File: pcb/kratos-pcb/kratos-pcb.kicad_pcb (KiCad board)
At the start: 2 copper layers, 100 x 100 mm, 28 parts, among them IC2 SN74HC595N, J1 Barrel_Jack_Switch_Pin3Ring, J2 Screw_Terminal_01x04, J3 Screw_Terminal_01x04, Q2 2N2222A, Q3 2N2222A, SW1 SW_Push, U1 ESP32-DEVKIT-V1, U2 ULN2803A, U3 ULN2803A

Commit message: kicad
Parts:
- C1: footprint Capacitor_THT:C_Disc_D3.0mm_W1.6mm_P2.50mm -> Capacitor_THT:CP_Radial_D4.0mm_P1.50mm
- moved Q3 52.7 mm to (164.3, 58.6), turned to 0 degrees
- moved Q2 50.8 mm to (153.0, 58.4), turned to 0 degrees
- moved R5 43.8 mm to (161.3, 64.8), turned to -90 degrees
- moved R4 43.1 mm to (149.9, 64.8), turned to -90 degrees
- moved R7 40.7 mm to (167.0, 69.8), turned to 90 degrees
- moved R6 35.0 mm to (155.6, 69.8), turned to 90 degrees
- moved IC2 24.2 mm to (142.9, 104.3), turned to -90 degrees
- moved U3 16.7 mm to (145.4, 88.3), turned to 90 degrees
- moved U2 13.4 mm to (168.3, 116.2), turned to 90 degrees
- moved C1 10.9 mm to (123.4, 68.6)
- moved C2 9.71 mm to (116.8, 62.9)
- moved R1 9.71 mm to (119.4, 59.1)
- moved VR1 9.71 mm to (123.8, 62.9)
- moved R2 9.55 mm to (132.1, 59.1)
- moved SW1 6.48 mm to (134.6, 139.7)

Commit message: ki
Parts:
- R7: value R -> 1k
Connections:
- C2 pad 1: Net-(VR1-VIN) -> +12V
- J1 pad 1: Net-(VR1-VIN) -> +12V
- LOCK_1 pad 1: unconnected-(LOCK_1-Pin_1-Pad1) -> +12V
- LOCK_1 pad 2: unconnected-(LOCK_1-Pin_2-Pad2) -> Net-(LOCK_1-Pin_2)
- LOCK_2 pad 1: unconnected-(LOCK_2-Pin_1-Pad1) -> +12V
- LOCK_2 pad 2: unconnected-(LOCK_2-Pin_2-Pad2) -> Net-(LOCK_2-Pin_2)
- Q2 pad 1: Net-(Q2-Pad1) -> GND
- Q2 pad 3: unconnected-(Q2-Pad3) -> Net-(LOCK_2-Pin_2)
- Q3 pad 1: Net-(Q3-Pad1) -> GND
- Q3 pad 3: unconnected-(Q3-Pad3) -> Net-(LOCK_1-Pin_2)
- VR1 pad 3: Net-(VR1-VIN) -> +12V
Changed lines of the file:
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@@
   (net 1 "+5V")
   (net 2 "GND")
-  (net 3 "Net-(VR1-VIN)")
+  (net 3 "+12V")
   (net 4 "DHT_DATA")
   (net 5 "Net-(FREE_OUTPUT1-Pin_1)")
@@
   (net 16 "Net-(Q2-Pad1)")
   (net 17 "Net-(Q2-Pad2)")
-  (net 18 "unconnected-(Q2-Pad3)")
+  (net 18 "Net-(LOCK_1-Pin_2)")
   (net 19 "Net-(Q3-Pad1)")
   (net 20 "Net-(Q3-Pad2)")
-  (net 21 "unconnected-(Q3-Pad3)")
+  (net 21 "Net-(LOCK_2-Pin_2)")
   (net 22 "Net-(VR1-ADJ)")
   (net 23 "unconnected-(R4-Pad2)")
@@
   (net 66 "Net-(J2-Pin_1)")
   (net 67 "Net-(J2-Pin_2)")
-  (net 68 "unconnected-(LOCK_1-Pin_1-Pad1)")
-  (net 69 "unconnected-(LOCK_1-Pin_2-Pad2)")
-  (net 70 "unconnected-(LOCK_2-Pin_1-Pad1)")
-  (net 71 "unconnected-(LOCK_2-Pin_2-Pad2)")
-  (net 72 "unconnected-(J1-Pad2)")
+  (net 68 "unconnected-(J1-Pad2)")
   (footprint "ULN2803A:ULN2803A" (layer "F.Cu")
     (at 168.275 116.205 90)
@@
       (stroke (width 0.1) (type solid)) (layer "F.Fab"))
     (pad "1" thru_hole rect (at 0 0 180) (size 3 3) (drill 1.52) (layers "*.Cu" "*.Mask")
-      (net 68 "unconnected-(LOCK_1-Pin_1-Pad1)") (pinfunction "Pin_1") (pintype "passive"))
+      (net 3 "+12V") (pinfunction "Pin_1") (pintype "passive"))
     (pad "2" thru_hole circle (at 5.08 0 180) (size 3 3) (drill 1.52) (layers "*.Cu" "*.Mask")
-      (net 69 "unconnected-(LOCK_1-Pin_2-Pad2)") (pinfunction "Pin_2") (pintype "passive"))
+      (net 18 "Net-(LOCK_1-Pin_2)") (pinfunction "Pin_2") (pintype "passive"))
     (model "${KICAD6_3DMODEL_DIR}/TerminalBlock.3dshapes/TerminalBlock_bornier-2_P5.08mm.wrl"
       (offset (xyz 2.539999962 0 0))
@@
       (stroke (width 0.2) (type solid)) (fill none) (layer "F.Fab"))
     (pad "1" thru_hole rect (at -2.54 2.33) (size 1.298 1.298) (drill 0.79) (layers "*.Cu" "*.Mask")
-      (net 19 "Net-(Q3-Pad1)") (pintype "passive") (solder_mask_margin 0.102))
+      (net 2 "GND") (pintype "passive") (solder_mask_margin 0.102))
     (pad "2" thru_hole circle (at 0 2.33) (size 1.298 1.298) (drill 0.79) (layers "*.Cu" "*.Mask")
       (net 20 "Net-(Q3-Pad2)") (pintype "passive") (solder_mask_margin 0.102))
     (pad "3" thru_hole circle (at 2.54 2.33) (size 1.298 1.298) (drill 0.79) (layers "*.Cu" "*.Mask")
-      (net 21 "unconnected-(Q3-Pad3)") (pintype "passive") (solder_mask_margin 0.102))
+      (net 18 "Net-(LOCK_1-Pin_2)") (pintype "passive") (solder_mask_margin 0.102))
     (model "${KIPRJMOD}/components/2N2222A/2N2222A.step"
       (offset (xyz 0 -2 6))
@@
       (net 1 "+5V") (pinfunction "VOUT") (pintype "output") (solder_mask_margin 0.102))
     (pad "3" thru_hole circle (at 2.54 0 180) (size 1.86 1.86) (drill 1.24) (layers "*.Cu" "*.Mask")
-      (net 3 "Net-(VR1-VIN)") (pinfunction "VIN") (pintype "input") (solder_mask_margin 0.102))
+      (net 3 "+12V") (pinfunction "VIN") (pintype "input") (solder_mask_margin 0.102))
     (model "${KIPRJMOD}/components/LM317T/LM317T.step"
       (offset (xyz 0 0 0))
@@
       (stroke (width 0.2) (type solid)) (fill none) (layer "F.Fab"))
     (pad "1" thru_hole rect (at -2.54 2.33) (size 1.298 1.298) (drill 0.79) (layers "*.Cu" "*.Mask")
-      (net 16 "Net-(Q2-Pad1)") (pintype "passive") (solder_mask_margin 0.102))
+      (net 2 "GND") (pintype "passive") (solder_mask_margin 0.102))
     (pad "2" thru_hole circle (at 0 2.33) (size 1.298 1.298) (drill 0.79) (layers "*.Cu" "*.Mask")
       (net 17 "Net-(Q2-Pad2)") (pintype "passive") (solder_mask_margin 0.102))
     (pad "3" thru_hole circle (at 2.54 2.33) (size 1.298 1.298) (drill 0.79) (layers "*.Cu" "*.Mask")
-      (net 18 "unconnected-(Q2-Pad3)") (pintype "passive") (solder_mask_margin 0.102))
+      (net 21 "Net-(LOCK_2-Pin_2)") (pintype "passive") (solder_mask_margin 0.102))
     (model "${KIPRJMOD}/components/2N2222A/2N2222A.step"
       (offset (xyz 0 -2 6.5))
@@
       (stroke (width 0.1) (type solid)) (layer "F.Fab"))
     (pad "1" thru_hole rect (at 0 0 180) (size 3 3) (drill 1.52) (layers "*.Cu" "*.Mask")
-      (net 70 "unconnected-(LOCK_2-Pin_1-Pad1)") (pinfunction "Pin_1") (pintype "passive"))
+      (net 3 "+12V") (pinfunction "Pin_1") (pintype "passive"))
     (pad "2" thru_hole circle (at 5.08 0 180) (size 3 3) (drill 1.52) (layers "*.Cu" "*.Mask")
-      (net 71 "unconnected-(LOCK_2-Pin_2-Pad2)") (pinfunction "Pin_2") (pintype "passive"))
+      (net 21 "Net-(LOCK_2-Pin_2)") (pinfunction "Pin_2") (pintype "passive"))
     (model "${KICAD6_3DMODEL_DIR}/TerminalBlock.3dshapes/TerminalBlock_bornier-2_P5.08mm.wrl"
       (offset (xyz 2.539999962 0 0))
@@
       (stroke (width 0.1) (type solid)) (layer "F.Fab"))
     (pad "1" thru_hole rect (at 0 0) (size 3.5 3.5) (drill oval 1 3) (layers "*.Cu" "*.Mask")
-      (net 3 "Net-(VR1-VIN)") (pintype "passive"))
+      (net 3 "+12V") (pintype "passive"))
     (pad "2" thru_hole roundrect (at -6 0) (size 3 3.5) (drill oval 1 3) (layers "*.Cu" "*.Mask") (roundrect_rratio 0.25)
-      (net 72 "unconnected-(J1-Pad2)") (pintype "passive+no_connect"))
+      (net 68 "unconnected-(J1-Pad2)") (pintype "passive+no_connect"))
     (pad "3" thru_hole roundrect (at -3 4.7) (size 3.5 3.5) (drill oval 3 1) (layers "*.Cu" "*.Mask") (roundrect_rratio 0.25)
       (net 2 "GND") (pintype "passive"))
@@
         (effects (font (size 1 1) (thickness 0.15)))
     )
-    (fp_text value "R" (at 2.54 1.92 90) (layer "F.Fab")
+    (fp_text value "1k" (at 2.54 1.92 90) (layer "F.Fab")
         (effects (font (size 1 1) (thickness 0.15)))
     )
@@
       (stroke (width 0.1) (type solid)) (layer "F.Fab"))
     (pad "1" thru_hole circle (at 0 0 270) (size 1.6 1.6) (drill 0.8) (layers "*.Cu" "*.Mask")
-      (net 3 "Net-(VR1-VIN)") (pintype "passive"))
+      (net 3 "+12V") (pintype "passive"))
     (pad "2" thru_hole circle (at 2.5 0 270) (size 1.6 1.6) (drill 0.8) (layers "*.Cu" "*.Mask")
       (net 2 "GND") (pintype "passive"))

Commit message: ## updatee
- gitignor
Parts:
- removed R4, R5: R, Resistor_THT:R_Axial_DIN0204_L3.6mm_D1.6mm_P5.08mm_Horizontal
- added LEDS1: Screw_Terminal_01x03, TerminalBlock_4Ucon:TerminalBlock_4Ucon_1x03_P3.50mm_Horizontal, F.Cu at (190.5, 80.3)
- R6: value R -> 1K
- moved LOCK_2 91.2 mm to (157.5, 48.3)
- moved LOCK_1 91.2 mm to (170.2, 48.3)
- moved SDOOR_1 42.0 mm to (147.3, 139.7), turned to 180 degrees
- moved SDOOR_2 32.2 mm to (160.0, 139.7), turned to 180 degrees
- moved U3 23.6 mm to (166.4, 77.5), turned to 0 degrees
- moved U2 22.5 mm to (146.1, 113.0), turned to 0 degrees
- moved J3 17.2 mm to (190.5, 132.1)
- moved IC2 12.9 mm to (142.2, 91.4)
- moved R6 12.8 mm to (149.9, 58.4), turned to 0 degrees
- moved R7 12.3 mm to (162.6, 58.4), turned to 0 degrees
- moved C1 10.5 mm to (113.3, 66.0)
- moved R8 9.09 mm to (104.1, 83.8)
- moved FAN1 8.26 mm to (167.6, 139.4)
- moved C2 6.29 mm to (112.4, 58.4)
- moved R2 6.29 mm to (127.6, 54.6)
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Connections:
- FAN1 pad 1: FAN_PWM -> VCC
- FAN1 pad 2: GND -> FAN_PWM
- IC2 pad 6: /EXPANSION DRIVERS/G -> LOCKER_1
- IC2 pad 7: /EXPANSION DRIVERS/H -> LOCKER_2
- LOCK_1 pad 1: +12V -> Net-(LOCK_1-Pin_1)
- LOCK_1 pad 2: Net-(LOCK_1-Pin_2) -> +12V
- LOCK_2 pad 1: +12V -> Net-(LOCK_2-Pin_1)
- LOCK_2 pad 2: Net-(LOCK_2-Pin_2) -> +12V
- Q2 pad 3: Net-(LOCK_2-Pin_2) -> Net-(LOCK_2-Pin_1)
- Q3 pad 3: Net-(LOCK_1-Pin_2) -> Net-(LOCK_1-Pin_1)
- U1 pad 10: GREEN-LED-2 -> unconnected-(U1-D19-Pad10)
- U1 pad 11: BLUE-LED-2 -> unconnected-(U1-D21-Pad11)
- U1 pad 15: SHIFT_SER -> DS
- U1 pad 26: SH_CP -> BLUE-LED-2
- U1 pad 28: DS -> GREEN-LED-2
- U1 pad 3: ST_CP -> unconnected-(U1-D15-Pad3)
- U1 pad 8: SHIFT_RCKL -> ST_CP
- U1 pad 9: SHIFT_SRCLOCK -> SH_CP
- U3 pad 1: /EXPANSION DRIVERS/H -> unconnected-(U3-I1-Pad1)
- U3 pad 14: LOCKER_1 -> Net-(LEDS1-Pin_3)
- U3 pad 15: LOCKER_2 -> Net-(LEDS1-Pin_2)
- U3 pad 16: Net-(FREE_OUTPUT1-Pin_3) -> Net-(LEDS1-Pin_1)
- U3 pad 17: Net-(FREE_OUTPUT1-Pin_2) -> unconnected-(U3-O2-Pad17)
- U3 pad 18: Net-(FREE_OUTPUT1-Pin_1) -> unconnected-(U3-O1-Pad18)
- U3 pad 2: /EXPANSION DRIVERS/G -> unconnected-(U3-I2-Pad2)

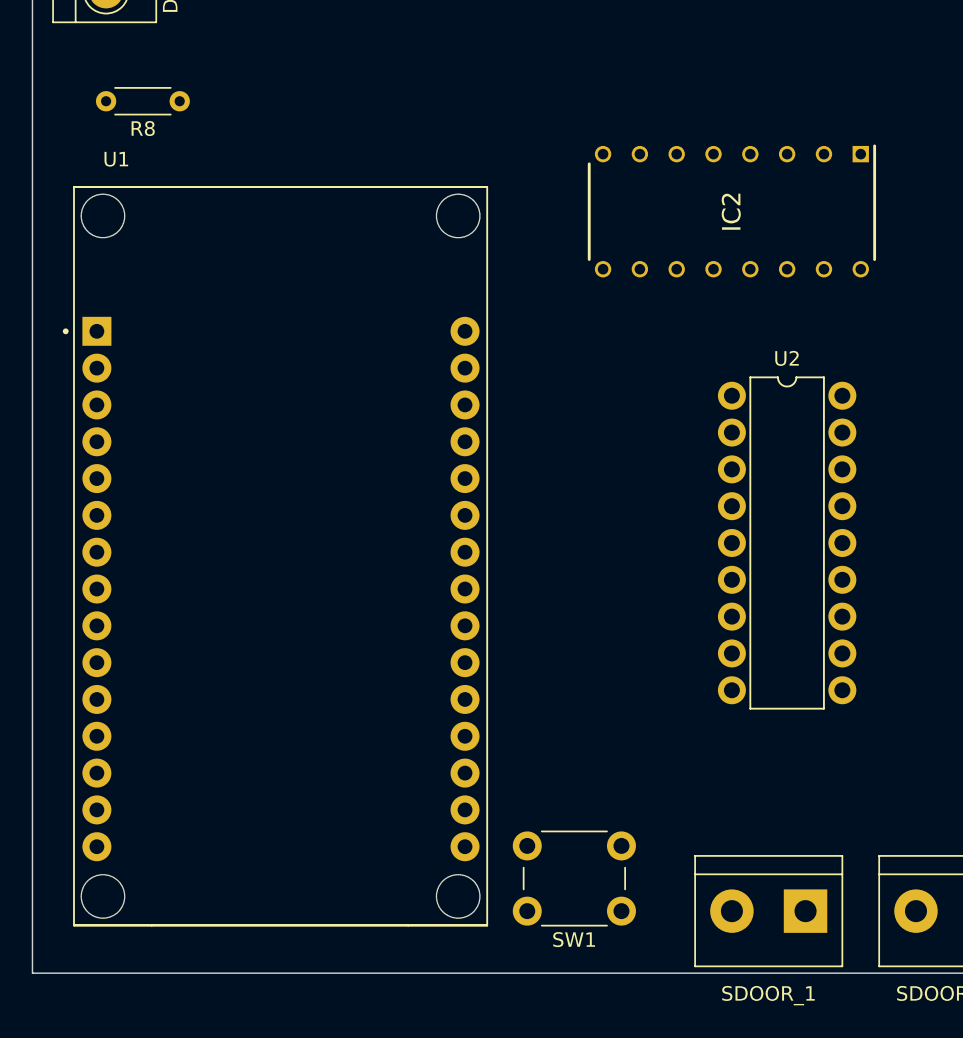
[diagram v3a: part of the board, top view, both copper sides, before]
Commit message: ### added - bitshift logic
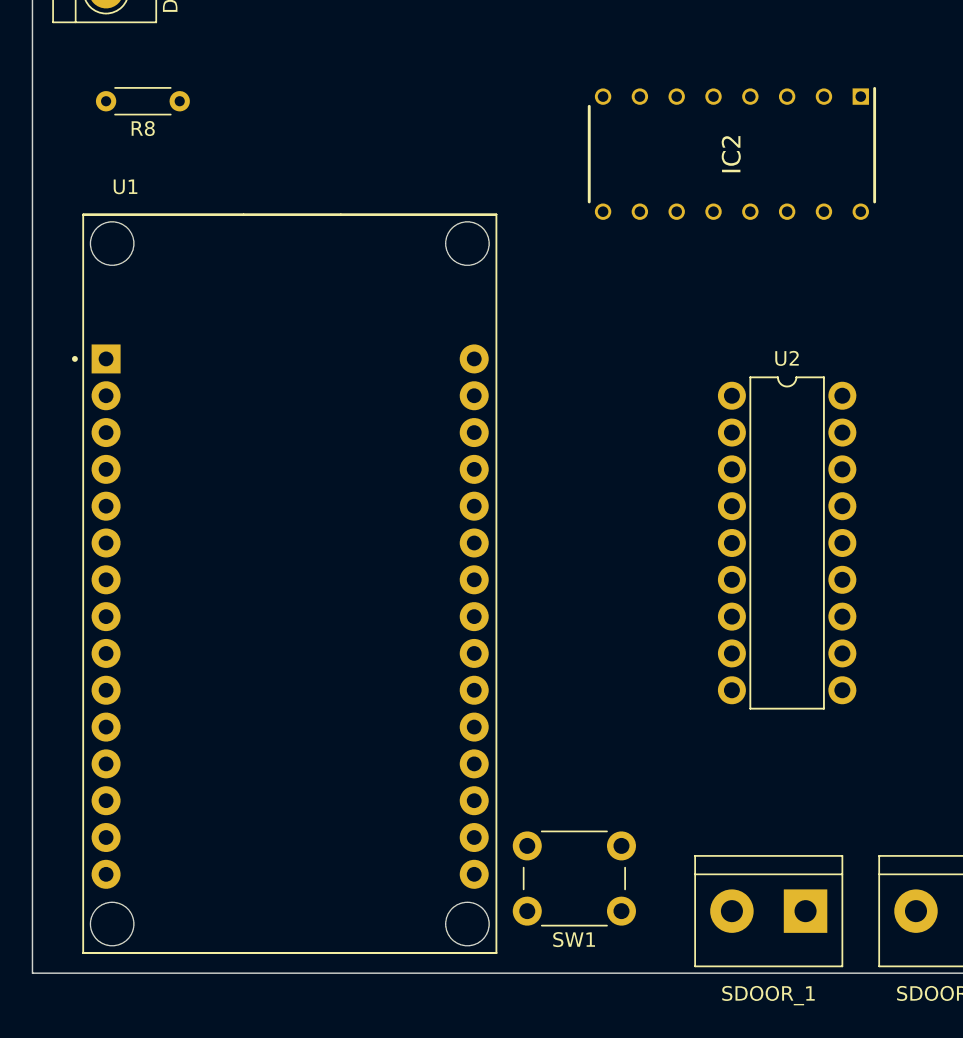
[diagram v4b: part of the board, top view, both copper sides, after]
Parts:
- moved IC2 3.97 mm to (142.2, 87.5)
- moved U1 2.01 mm to (111.8, 117.1)
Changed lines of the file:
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@@
   )
   (footprint "ESP32-DEVKIT-V1:MODULE_ESP32_DEVKIT_V1" (layer "F.Cu")
-    (at 111.125 115.21)
+    (at 111.76 117.115)
     (property "Availability" "Not in stock")
     (property "Check_prices" "https://www.snapeda.com/parts/ESP32-DEVKIT-V1/Do+it/view-part/?ref=eda")
@@
       (polygon
         (pts
-          (xy 102.215 134.195)
-          (xy 119.905 134.195)
-          (xy 119.905 140.685)
-          (xy 102.215 140.685)
+          (xy 102.85 136.1)
+          (xy 120.54 136.1)
+          (xy 120.54 142.59)
+          (xy 102.85 142.59)
         )
       )
@@
       (polygon
         (pts
-          (xy 102.215 134.195)
-          (xy 119.905 134.195)
-          (xy 119.905 140.685)
-          (xy 102.215 140.685)
+          (xy 102.85 136.1)
+          (xy 120.54 136.1)
+          (xy 120.54 142.59)
+          (xy 102.85 142.59)
         )
       )
@@
       (polygon
         (pts
-          (xy 102.215 134.195)
-          (xy 119.905 134.195)
-          (xy 119.905 140.685)
-          (xy 102.215 140.685)
+          (xy 102.85 136.1)
+          (xy 120.54 136.1)
+          (xy 120.54 142.59)
+          (xy 102.85 142.59)
         )
       )
@@
   )
   (footprint "SN74HC595N:DIP794W53P254L1930H508Q16N" (layer "F.Cu")
-    (at 142.24 91.44 -90)
+    (at 142.24 87.47 -90)
     (descr "N (R-PDIP-T16)")
     (tags "Integrated Circuit")

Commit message: ### added
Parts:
- removed FREE_OUTPUT1: Screw_Terminal_01x03, TerminalBlock_4Ucon:TerminalBlock_4Ucon_1x03_P3.50mm_Horizontal
- removed J2, J3: Screw_Terminal_01x04, TerminalBlock:TerminalBlock_bornier-4_P5.08mm
- added LED-RGB-1.1: Screw_Terminal_01x02, TerminalBlock:TerminalBlock_bornier-2_P5.08mm, F.Cu at (189.6, 93.0)
- added LED-RGB-1.2: Screw_Terminal_01x02, TerminalBlock:TerminalBlock_bornier-2_P5.08mm, F.Cu at (189.7, 79.0)
- added LED-RGB-2.1: Screw_Terminal_01x02, TerminalBlock:TerminalBlock_bornier-2_P5.08mm, F.Cu at (189.7, 68.3)
- added LED-RGB-2.2: Screw_Terminal_01x02, TerminalBlock:TerminalBlock_bornier-2_P5.08mm, F.Cu at (189.9, 57.0)
- added REF**: PinHeader_1x01_P1.00mm_Vertical, Connector_PinHeader_1.00mm:PinHeader_1x01_P1.00mm_Vertical, F.Cu at (128.0, 92.2)
- added REF**: PinHeader_1x01_P1.00mm_Vertical, Connector_PinHeader_1.00mm:PinHeader_1x01_P1.00mm_Vertical, F.Cu at (162.3, 56.9)
- added REF**: PinHeader_1x01_P1.00mm_Vertical, Connector_PinHeader_1.00mm:PinHeader_1x01_P1.00mm_Vertical, F.Cu at (165.1, 45.7)
- added REF**: PinHeader_1x01_P1.00mm_Vertical, Connector_PinHeader_1.00mm:PinHeader_1x01_P1.00mm_Vertical, F.Cu at (119.1, 66.0)
- added REF**: PinHeader_1x01_P1.00mm_Vertical, Connector_PinHeader_1.00mm:PinHeader_1x01_P1.00mm_Vertical, F.Cu at (170.7, 84.8)
- added REF**: PinHeader_1x01_P1.00mm_Vertical, Connector_PinHeader_1.00mm:PinHeader_1x01_P1.00mm_Vertical, F.Cu at (162.1, 52.3)
- added REF**: PinHeader_1x01_P1.00mm_Vertical, Connector_PinHeader_1.00mm:PinHeader_1x01_P1.00mm_Vertical, F.Cu at (113.3, 99.6)
- added RFID1: Conn_01x04_Pin, Connector_PinHeader_2.00mm:PinHeader_1x04_P2.00mm_Vertical, F.Cu at (119.1, 45.6)
- moved SW1 100.5 mm to (170.3, 45.8), turned to 0 degrees
- moved LEDS1 92.6 mm to (98.0, 75.8)
- moved RELAYS1 91.7 mm to (98.0, 63.6), turned to -90 degrees
- moved LOCK_1 90.9 mm to (151.4, 137.2), turned to 0 degrees
- moved LOCK_2 90.8 mm to (140.0, 137.4), turned to 0 degrees
- moved J1 79.2 mm to (102.7, 129.9), turned to 90 degrees
- moved Q2 74.0 mm to (139.9, 125.7)
- moved Q3 73.9 mm to (154.3, 126.0)
- moved C2 65.7 mm to (103.8, 123.6), turned to 0 degrees
- moved R1 64.1 mm to (98.9, 116.6), turned to 90 degrees
- moved VR1 60.2 mm to (103.8, 116.6), turned to -90 degrees
- moved R6 59.5 mm to (139.7, 117.1), turned to -90 degrees
- moved R7 58.0 mm to (154.1, 115.8), turned to -90 degrees
- moved U1 58.0 mm to (145.4, 69.9)
- moved R2 56.7 mm to (103.9, 106.1)
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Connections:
- FAN1 pad 1: VCC -> +5V
- LOCK_1 pad 1: Net-(LOCK_1-Pin_1) -> +12V
- LOCK_1 pad 2: +12V -> Net-(LOCK_1-Pin_2)
- LOCK_2 pad 1: Net-(LOCK_2-Pin_1) -> +12V
- LOCK_2 pad 2: +12V -> Net-(LOCK_2-Pin_2)
- Q2 pad 3: Net-(LOCK_2-Pin_1) -> Net-(LOCK_2-Pin_2)
- Q3 pad 3: Net-(LOCK_1-Pin_1) -> Net-(LOCK_1-Pin_2)
- R8 pad 1: +3V3 -> +3.3V
- U1 pad 21: BLUE-LED -> FAN_PWM_DRIVER
- U1 pad 22: GREEN-LED -> BLUE-LED
- U1 pad 23: RED-LED -> GREEN-LED
- U1 pad 25: FAN_PWM_DRIVER -> RED-LED
- U2 pad 1: RED-LED -> GREEN-LED-2
- U2 pad 2: GREEN-LED -> RED-LED-2
- U2 pad 3: BLUE-LED -> BLUE-LED-2
- U2 pad 4: RED-LED-2 -> RED-LED
- U2 pad 5: GREEN-LED-2 -> GREEN-LED
- U2 pad 6: BLUE-LED-2 -> BLUE-LED
- U3 pad 11: Net-(RELAYS1-Pin_3) -> Net-(RELAYS1-Pin_1)
- U3 pad 13: Net-(RELAYS1-Pin_1) -> Net-(RELAYS1-Pin_3)
- U3 pad 14: Net-(LEDS1-Pin_3) -> Net-(LEDS1-Pin_1)
- U3 pad 16: Net-(LEDS1-Pin_1) -> Net-(LEDS1-Pin_3)
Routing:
- net +5V: track 0.00 -> 213.6 mm
- net GND: track 0.00 -> 196.2 mm
- net +3.3V: track 0.00 -> 133.0 mm
- net +12V: track 0.00 -> 66.8 mm
- net Net-(U1-EN): track 0.00 -> 61.1 mm
- net SDOOR1: track 0.00 -> 59.5 mm
- net LOCKER_1: track 0.00 -> 53.8 mm
- net SDOOR2: track 0.00 -> 48.5 mm
- net LOCKER_2: track 0.00 -> 41.1 mm
- net DHT_DATA: track 0.00 -> 38.7 mm
- net FAN_PWM: track 0.00 -> 32.0 mm
- net Net-(LED-RGB-1.1-Pin_2): track 0.00 -> 25.5 mm
- net DS: track 0.00 -> 21.0 mm
- net Net-(LED-RGB-1.2-Pin_1): track 0.00 -> 19.7 mm
- net Net-(LED-RGB-2.2-Pin_2): track 0.00 -> 19.1 mm
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
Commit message: removed
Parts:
- removed REF** (x7): PinHeader_1x01_P1.00mm_Vertical, Connector_PinHeader_1.00mm:PinHeader_1x01_P1.00mm_Vertical
- moved R6 6.48 mm to (144.0, 122.0)
- moved R7 6.26 mm to (155.1, 122.0)
- moved Q2 5.28 mm to (144.0, 129.0)
- moved SW1 3.38 mm to (166.9, 45.8)
- moved Q3 3.13 mm to (155.1, 129.0)
- moved R2 2.78 mm to (105.4, 108.5)
- moved LOCK_1 2.64 mm to (152.6, 139.5)
- moved LOCK_2 2.64 mm to (141.2, 139.7)
- moved R1 1.47 mm to (100.3, 116.6)
- moved SDOOR_2 1.05 mm to (189.7, 111.3)
- moved SDOOR_1 0.36 mm to (189.7, 127.3)
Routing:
- net +5V: track 213.6 -> 0.81 mm
- net GND: track 196.2 -> 0.34 mm
- net +3.3V: track 133.0 -> 0.04 mm
- net +12V: track 66.8 -> 0.15 mm
- net Net-(U1-EN): track 61.1 -> 0.05 mm
- net SDOOR1: track 59.5 -> 0.00 mm
- net LOCKER_1: track 53.8 -> 0.00 mm
- net SDOOR2: track 48.5 -> 0.00 mm
- net LOCKER_2: track 41.1 -> 0.00 mm
- net DHT_DATA: track 38.7 -> 0.00 mm
- net FAN_PWM: track 32.0 -> 0.00 mm
- net Net-(LED-RGB-1.1-Pin_2): track 25.5 -> 0.00 mm
- net DS: track 21.0 -> 0.00 mm
- net Net-(LED-RGB-1.2-Pin_1): track 19.7 -> 0.00 mm
- net Net-(LED-RGB-2.2-Pin_2): track 19.1 -> 0.00 mm
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
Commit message: ### modify
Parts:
- moved RFID1 7.83 mm to (111.3, 46.0), turned to 90 degrees
- moved R2 7.01 mm to (100.3, 103.6), turned to -90 degrees
- moved SDOOR_2 4.72 mm to (186.9, 115.1), turned to 90 degrees
- moved SDOOR_1 3.05 mm to (186.7, 127.3)
- moved LOCK_2 1.80 mm to (141.5, 137.9)
- moved LOCK_1 1.58 mm to (152.7, 137.9)
- moved IC2 0.44 mm to (123.3, 79.2)
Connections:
- IC2 pad 15: unconnected-(IC2-QA-Pad15) -> /EXPANSION DRIVERS/A
- RFID1 pad 2: RFID - TX -> RFID - RX
- RFID1 pad 3: RFID - RX -> RFID - TX
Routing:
- net +5V: track 0.81 -> 313.2 mm
- net +3.3V: track 0.04 -> 148.6 mm
- net +12V: track 0.15 -> 92.4 mm
- net SDOOR1: track 0.00 -> 59.4 mm
- net LOCKER_1: track 0.00 -> 59.0 mm
- net Net-(U1-EN): track 0.05 -> 57.4 mm
- net SDOOR2: track 0.00 -> 54.7 mm
- net LOCKER_2: track 0.00 -> 47.5 mm
- net DHT_DATA: track 0.00 -> 38.7 mm
- net (no net): track 0.00 -> 38.6 mm
- net RFID - RX: track 0.00 -> 33.4 mm
- net FAN_PWM: track 0.00 -> 31.8 mm
- net RFID - TX: track 0.00 -> 30.6 mm
- net Net-(LED-RGB-1.1-Pin_2): track 0.00 -> 23.2 mm
- net Net-(LED-RGB-1.2-Pin_1): track 0.00 -> 19.7 mm
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- added copper zone on B.Cu, net +12V
- added copper zone on B.Cu, net +3.3V
- added copper zone on F.Cu, net +5V
- added copper zone on B.Cu, net GND
- added copper zone on F.Cu, net GND
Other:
- board outline removed
- board text added: "0.1 mm"
- board text added: "0.3 mm"
- board text added: "0.5 mm"
- board text added: "1.0 mm"
- board text added: "KRATOS V1 by Gustavo Abdon"
